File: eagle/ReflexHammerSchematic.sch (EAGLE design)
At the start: 9 parts

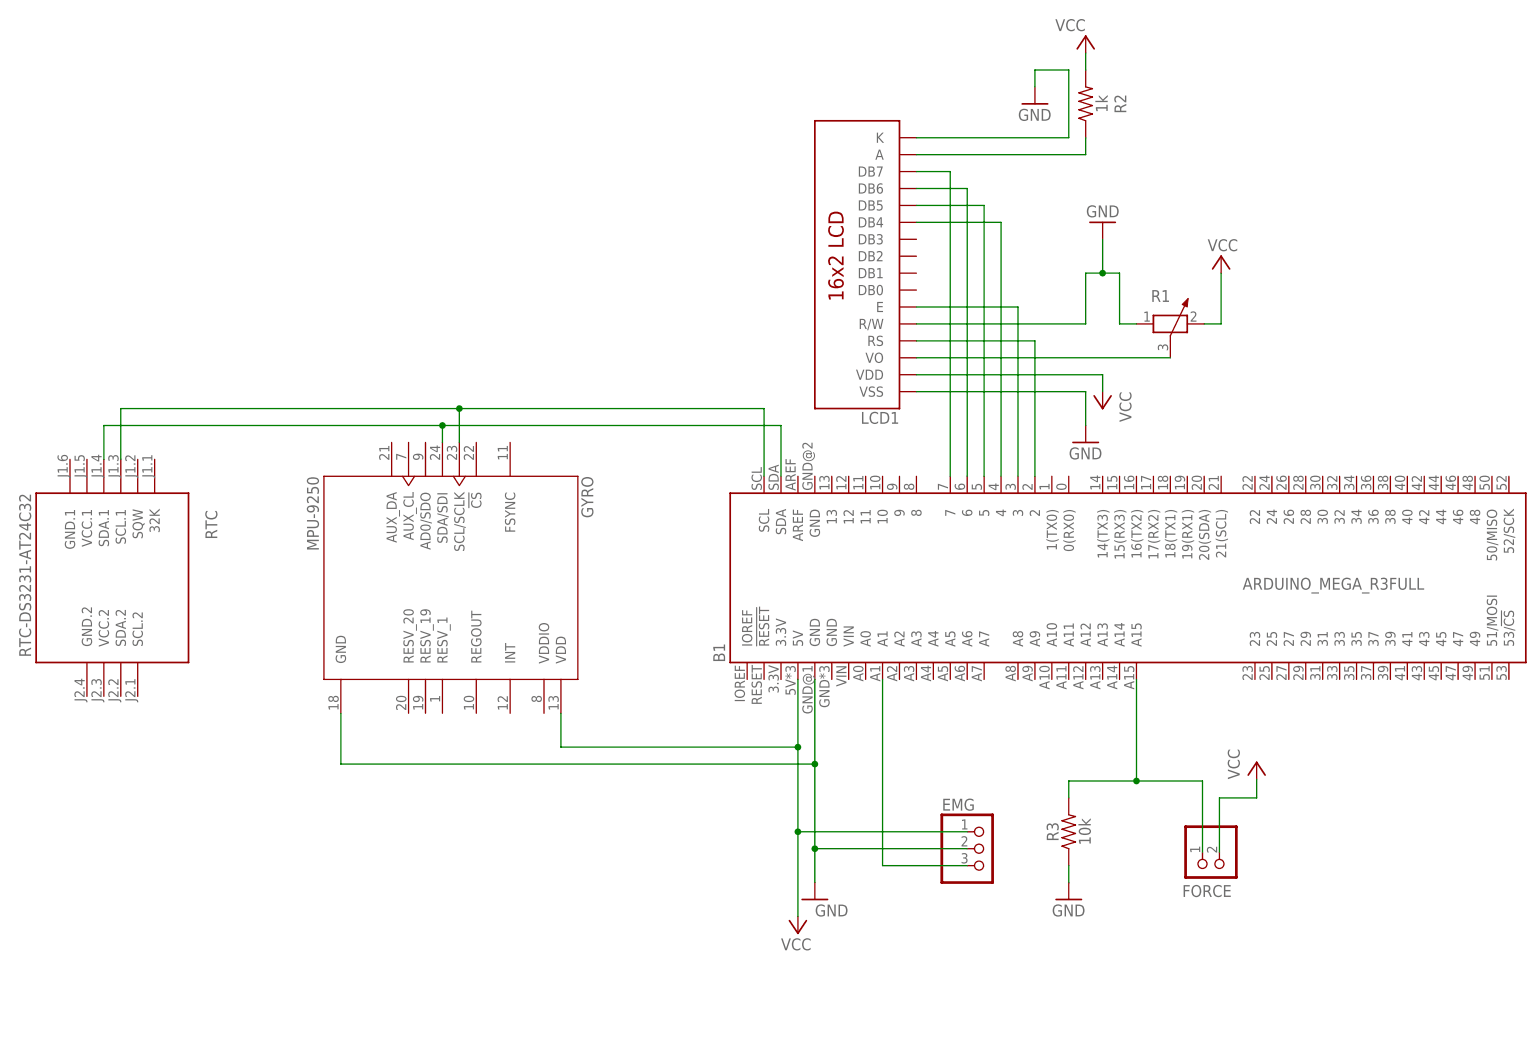
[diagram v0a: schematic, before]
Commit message: Add files via upload
The new schematic removes the LCD display and uses the serial monitor to gather data.
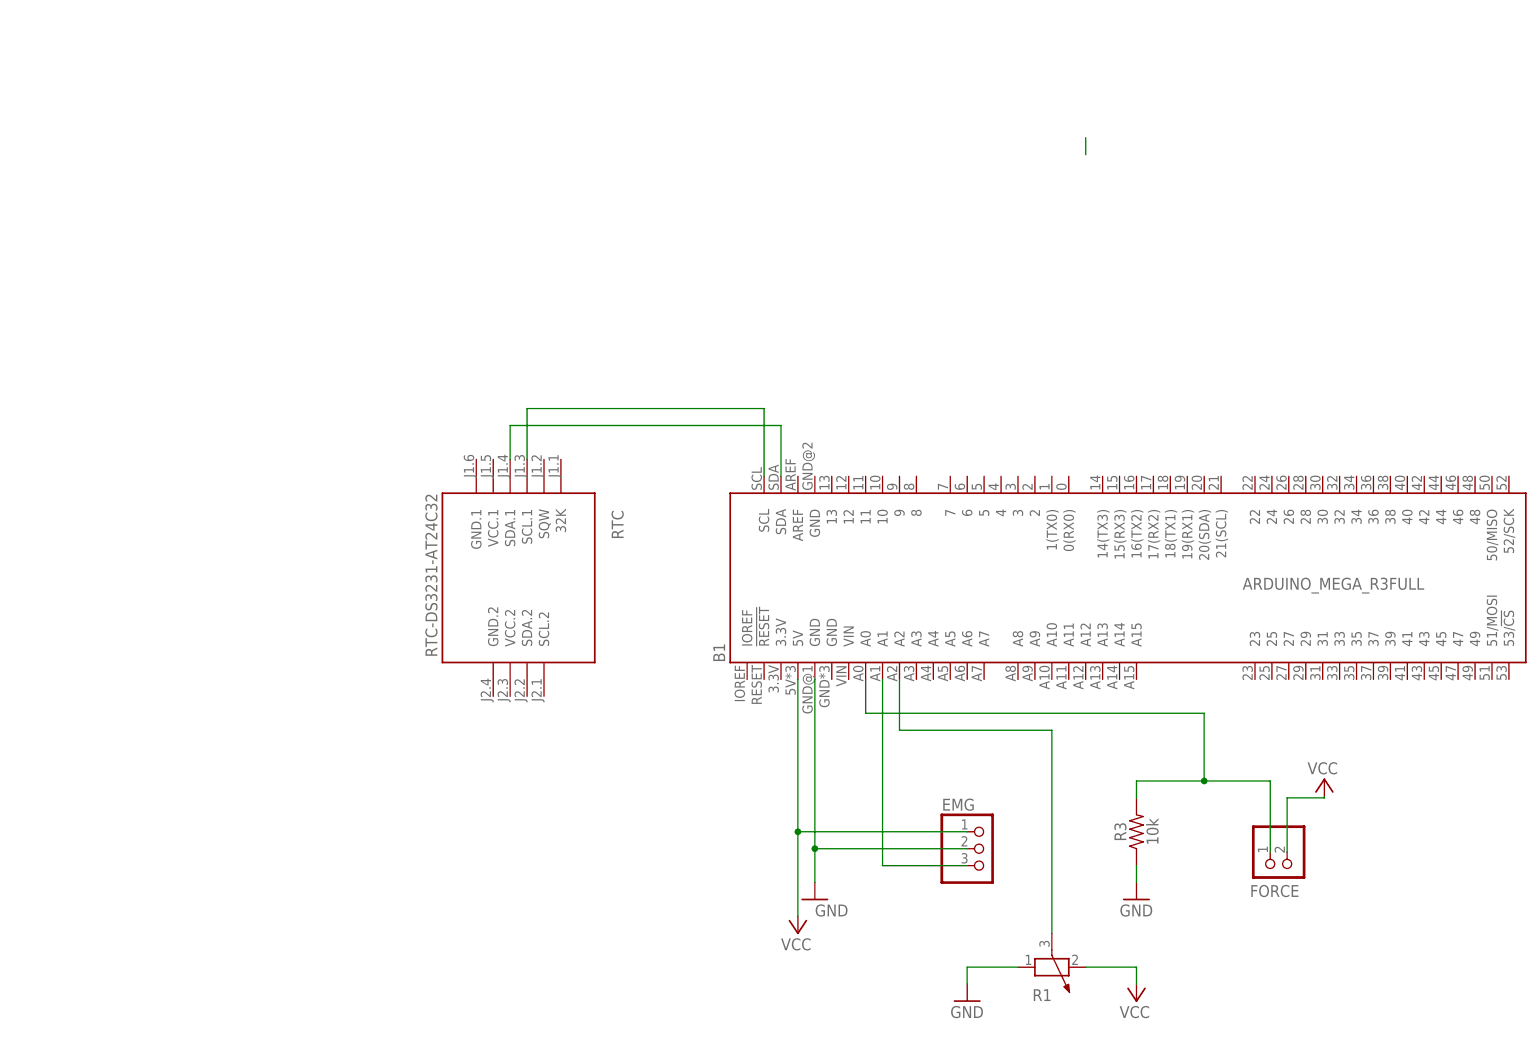
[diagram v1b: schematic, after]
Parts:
- removed GYRO: MPU-9250, MPU-9250:MPU-9250
- removed LCD1: LCD-16X2NOHOLES, SparkFun-Displays:LCD-16X2NOHOLES
- removed R2: 1k, SparkFun-Resistors:1KOHM-HORIZ-1/4W-1%
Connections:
- removed net N$10: B1.3, LCD1.E
- removed net N$13: LCD1.VO, R1.3
- removed net N$4: B1.7, LCD1.DB7
- removed net N$5: LCD1.A, R2.1
- removed net N$6: B1.6, LCD1.DB6
- removed net N$7: B1.5, LCD1.DB5
- removed net N$8: B1.4, LCD1.DB4
- removed net N$9: B1.A15, FORCE.2, R3.2
- new net N$3: B1.A2, R1.3
- net GND: no longer GYRO.GND, LCD1.K, LCD1.R/W, LCD1.VSS
- net N$1: now also B1.A0, FORCE.2, R3.2; no longer B1.2, LCD1.RS
- net N$14: no longer GYRO.SDA/SDI
- net N$15: no longer GYRO.SCL/SCLK
- net VCC: no longer GYRO.VDD, LCD1.VDD, R2.2
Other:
- moved on the sheet: FORCE, R1, R3, RTC
